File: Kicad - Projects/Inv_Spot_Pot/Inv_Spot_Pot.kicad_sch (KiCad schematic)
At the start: 29 parts, among them J1 Screw_Terminal_01x03, J2 PWM, J4 Current_Sense, J5 Temperature_Sense, Q1 40T120, Q2 40T120, T1 Transformer_1P_2S

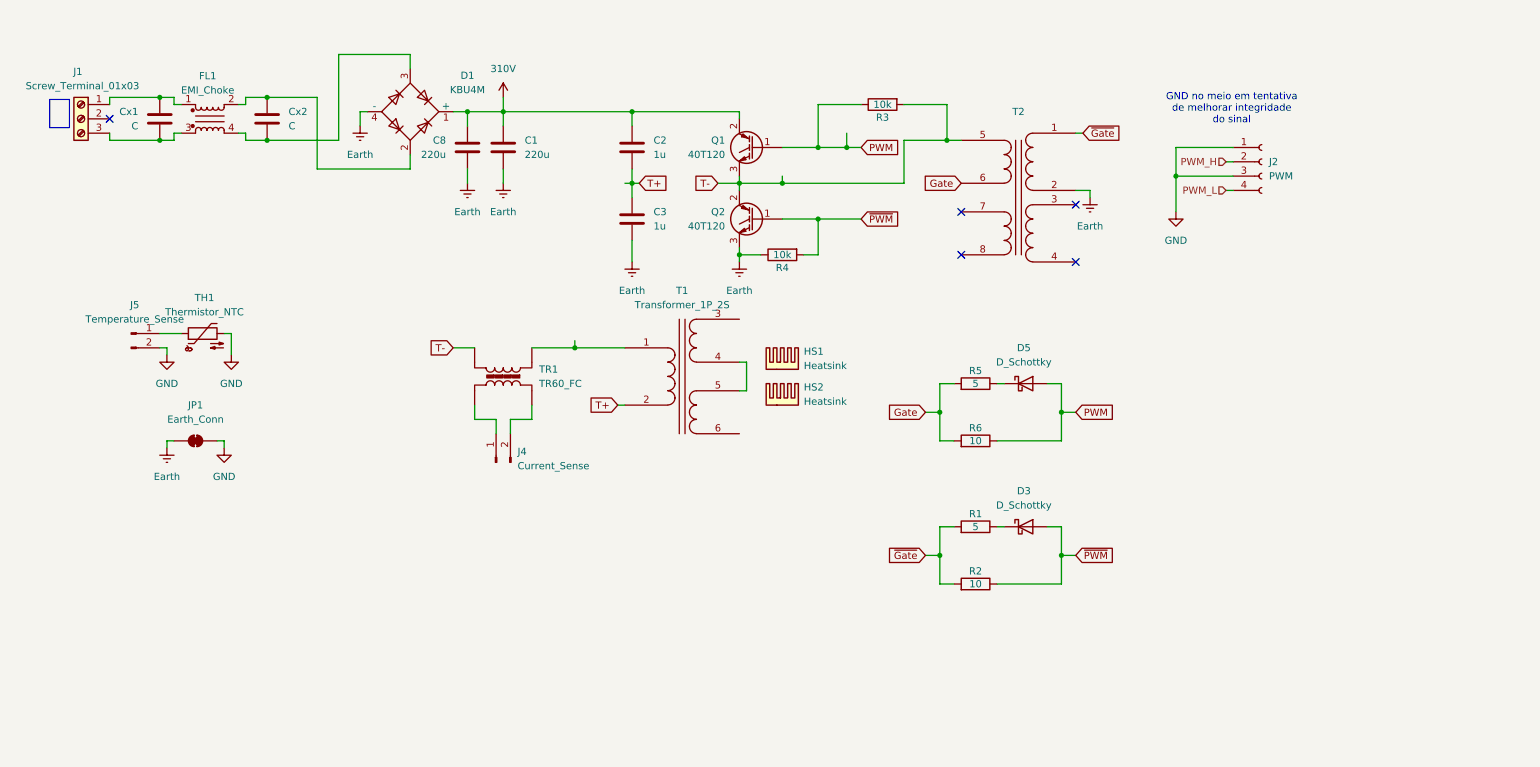
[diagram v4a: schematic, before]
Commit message: General Polishing
Removidos furos dos dissipadores que não serão utilizados, aberto espaço previsto para relé e circuito de tensão auxiliar

Falta ainda corrigir o footprint do transformador (bobinar) e a placa base de display que será utilizada
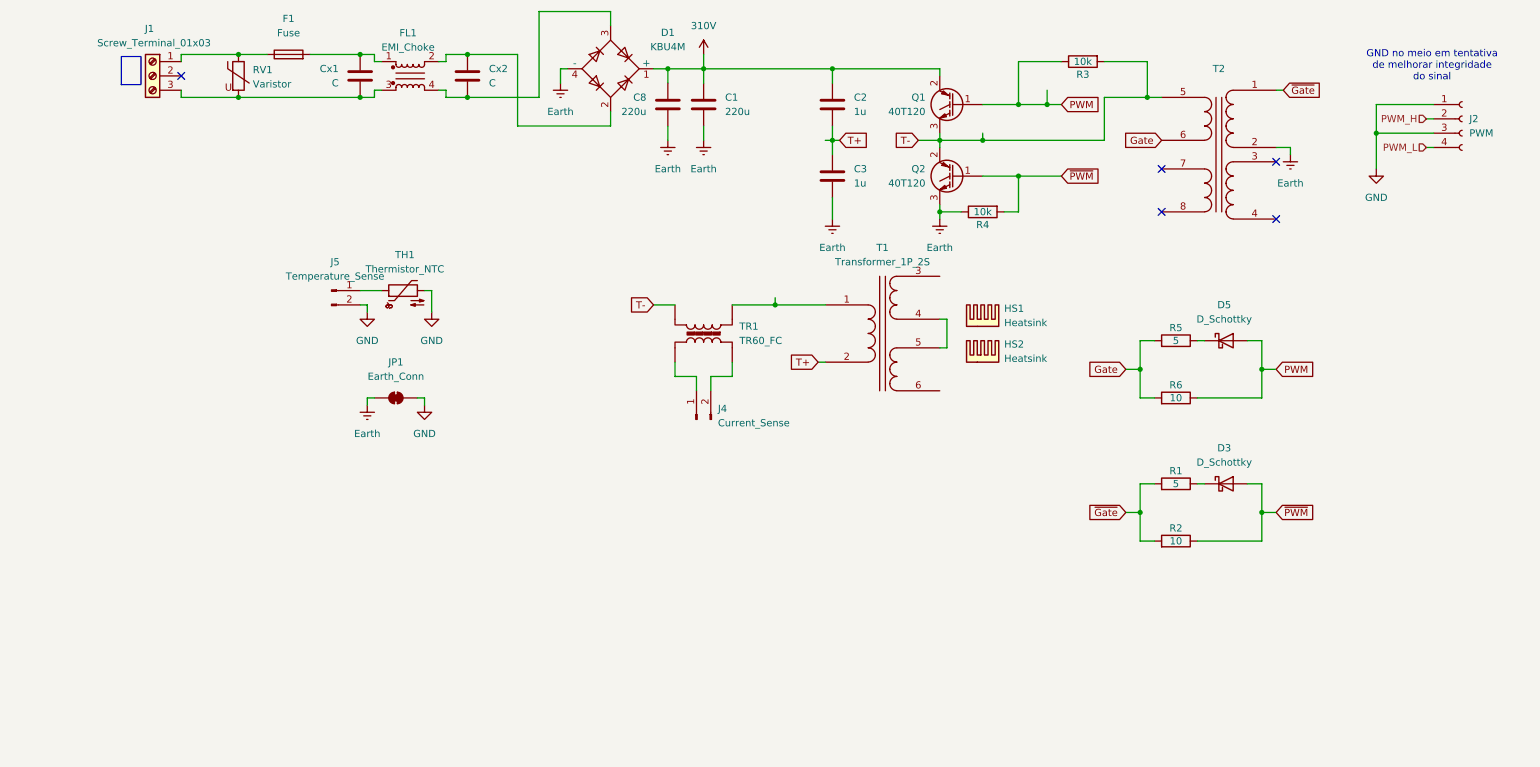
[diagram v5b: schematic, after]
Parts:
- added F1: Fuse, Fuse:Fuseholder_Clip-5x20mm_Schurter_CQM_Inline_P20.60x5.00mm_D1.00mm_Horizontal, symbol Device:Fuse
- added RV1: Varistor, Varistor:RV_Disc_D7mm_W3.4mm_P5mm, symbol Device:Varistor
- J2: footprint Connector_JST:JST_VH_B4P-VH-B_1x04_P3.96mm_Vertical -> Connector_PinHeader_2.00mm:PinHeader_1x04_P2.00mm_Vertical
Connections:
- net at Cx1.1, FL1.1: now also F1.2; no longer J1.1 (Pin_1)
- net at Cx1.2, FL1.3, J1.3 (Pin_3): now also RV1.2
- new net: F1.1, J1.1 (Pin_1), RV1.1
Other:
- moved on the sheet: C1, C2, C3, C8, Cx1, Cx2, D1, D3, D5, FL1, HS1, HS2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

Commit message: Adicionando Fonte Auxiliar
Fonte auxiliar com topologia flyback dimencionada, falta criar o footprint do transformador, abrir o espaço na placa e finalizar o roteamento dos componentes
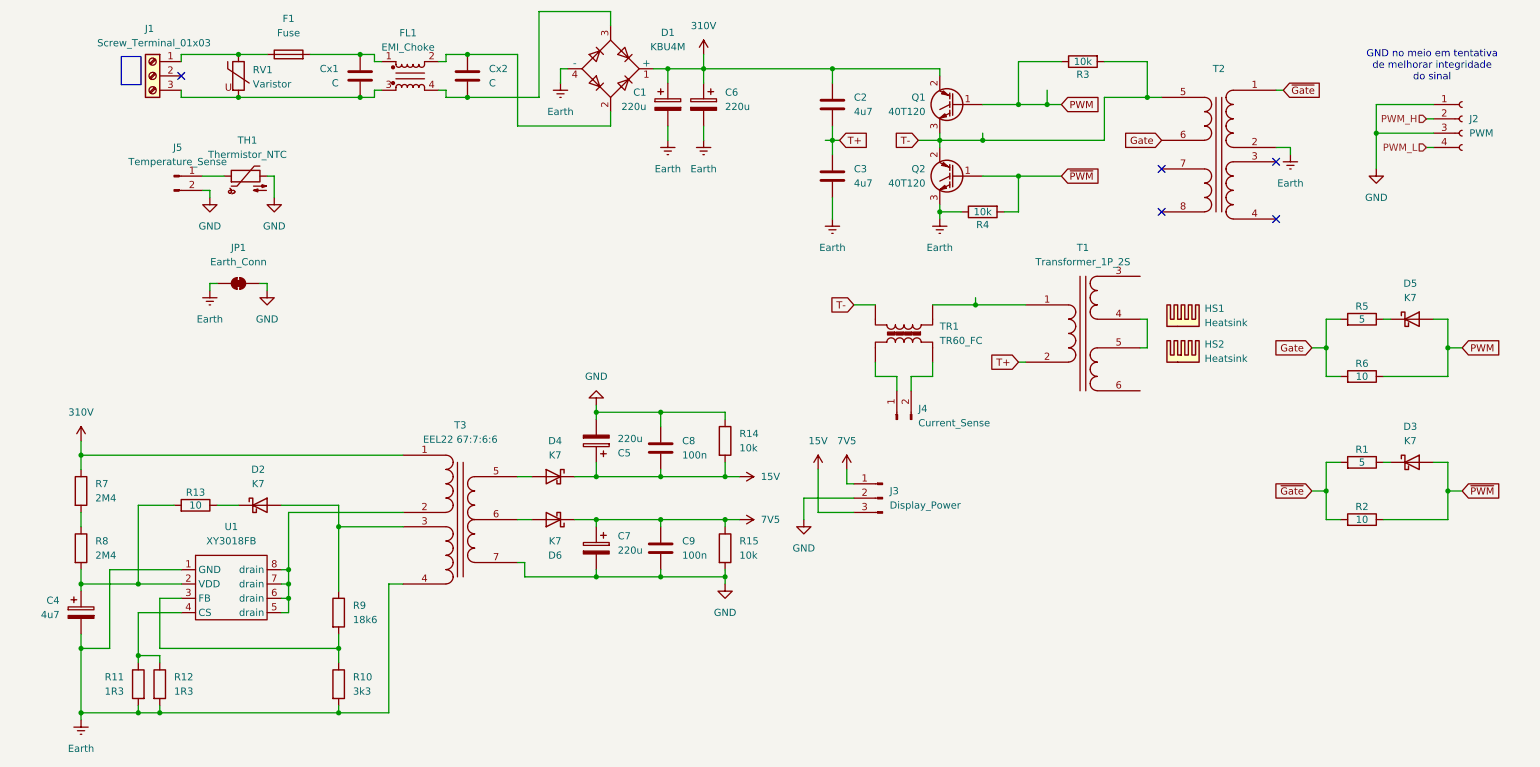
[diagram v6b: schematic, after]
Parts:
- removed C1: 220u, Capacitor_THT:C_Radial_D16.0mm_H25.0mm_P7.50mm, symbol Device:C
- added C1, C6: 220u, Capacitor_THT:C_Radial_D16.0mm_H25.0mm_P7.50mm, symbol Device:C_Polarized
- added C4: 4u7, Capacitor_THT:CP_Radial_D8.0mm_P3.50mm, symbol Device:C_Polarized
- added C5, C7: 220u, Capacitor_THT:CP_Radial_D8.0mm_P3.50mm, symbol Device:C_Polarized
- added C9: 100n, Capacitor_SMD:C_1206_3216Metric_Pad1.33x1.80mm_HandSolder, symbol Device:C
- added D2, D4, D6: K7, Diode_SMD:D_SOD-123F, symbol Device:D_Schottky
- added J3: Display_Power, Connector_PinHeader_2.00mm:PinHeader_1x03_P2.00mm_Vertical, symbol Connector:Conn_01x03_Pin
- added R10: 3k3, Resistor_SMD:R_1206_3216Metric_Pad1.30x1.75mm_HandSolder, symbol Device:R
- added R11, R12: 1R3, Resistor_SMD:R_1206_3216Metric_Pad1.30x1.75mm_HandSolder, symbol Device:R
- added R13: 10, Resistor_SMD:R_1206_3216Metric_Pad1.30x1.75mm_HandSolder, symbol Device:R
- added R14, R15: 10k, Resistor_SMD:R_1206_3216Metric_Pad1.30x1.75mm_HandSolder, symbol Device:R
- added R7, R8: 2M4, Resistor_SMD:R_1206_3216Metric_Pad1.30x1.75mm_HandSolder, symbol Device:R
- added R9: 18k6, Resistor_SMD:R_1206_3216Metric_Pad1.30x1.75mm_HandSolder, symbol Device:R
- added T3: EEL22 67:7:6:6, symbol Custom_Transformers:Transformer_1P_3S
- added U1: XY3018FB, Package_SO:SOIC-8_3.9x4.9mm_P1.27mm, symbol Custom_ICs:XY3018FB
- C2, C3: value 1u -> 4u7
- C8: value 220u -> 100n; footprint Capacitor_THT:C_Radial_D16.0mm_H25.0mm_P7.50mm -> Capacitor_SMD:C_1206_3216Metric_Pad1.33x1.80mm_HandSolder
- D3, D5: value D_Schottky -> K7
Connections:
- net 310V: now also C1.1, C6.1, R7.1, T3.1; no longer C8.1
- net Earth: now also C1.2, C4.2, C6.2, R10.2, R11.2, R12.2, T3.4, U1.1 (GND); no longer C8.2
- net GND: now also C8.1, C5.2, C7.2, C9.2, J3.2 (Pin_2), R14.1, R15.2, T3.7
- new net: D2.2 (A), R9.1, T3.3
- new net: R10.1, R9.2, U1.3 (FB)
- new net: D6.2 (A), T3.6
- new net: D2.1 (K), R13.1
- new net: C4.1, R13.2, R8.2, U1.2 (VDD)
- new net: T3.2, U1.5 (drain), U1.6 (drain), U1.7 (drain), U1.8 (drain)
- new net: D4.2 (A), T3.5
- new net: R11.1, R12.1, U1.4 (CS)
- new net: R7.2, R8.1
- new net 15V: C5.1, C8.2, D4.1 (K), J3.3 (Pin_3), R14.2
- new net 7V5: C7.1, C9.1, D6.1 (K), J3.1 (Pin_1), R15.1
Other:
- moved on the sheet: D3, D5, HS1, HS2, J4, J5, JP1, R1, R2, R5, R6, T1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

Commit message: Adicionado Flyback (WIP)
Adicionado circuito auxiliar flyback - footprint ocupa bastante espaço e aumenta significativamente a altura da placa.

Revendo layout para tentar melhorar o particionamento da placa
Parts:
- added C10: 47u, Capacitor_THT:CP_Radial_D8.0mm_P3.50mm, symbol Device:C_Polarized
- R7, R8: footprint Resistor_SMD:R_1206_3216Metric_Pad1.30x1.75mm_HandSolder -> Resistor_THT:R_Axial_DIN0309_L9.0mm_D3.2mm_P12.70mm_Horizontal
- T3: footprint (none) -> Transformer_THT:Custom_Transformer-10P-EEL22_EE30_7
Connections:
- net 15V: now also C7.1, C9.1, D6.1 (K), J3.1 (Pin_1), R15.1; no longer C5.1, C8.2, D4.1 (K), J3.3 (Pin_3), R14.2
- net 310V: now also C10.1
- net 7V5: now also C5.1, C8.2, D4.1 (K), J3.3 (Pin_3), R14.2; no longer C7.1, C9.1, D6.1 (K), J3.1 (Pin_1), R15.1
- net Earth: now also C10.2
- net GND: now also T3.6; no longer T3.7
- net at D6.2 (A): now also T3.9; no longer T3.6
- net at D4.2 (A): now also T3.7; no longer T3.5
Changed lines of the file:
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@@
 	(wire
 		(pts
+			(xy 19.05 139.7) (xy 19.05 140.97)
+		)
+		(stroke
+			(width 0)
+			(type default)
+		)
+	)
+	(wire
+		(pts
 			(xy 118.11 50.8) (xy 118.11 53.34)
 		)
@@
 	(wire
 		(pts
+			(xy 19.05 132.08) (xy 19.05 129.54)
+		)
+		(stroke
+			(width 0)
+			(type default)
+		)
+	)
+	(wire
+		(pts
 			(xy 176.53 72.39) (xy 176.53 73.66)
 		)
@@
 	(wire
 		(pts
+			(xy 19.05 129.54) (xy 24.13 129.54)
+		)
+		(stroke
+			(width 0)
+			(type default)
+		)
+	)
+	(wire
+		(pts
 			(xy 157.48 73.66) (xy 158.75 73.66)
 		)
@@
 			)
 		)
-		(property "Value" "15V"
+		(property "Value" "7V5"
 			(at 144.78 133.3499 90)
 			(effects
@@
 			)
 		)
-		(property "Value" "7V5"
+		(property "Value" "15V"
 			(at 160.02 127 0)
 			(effects
@@
 			)
 		)
-		(property "Footprint" ""
+		(property "Footprint" "Transformer_THT:Custom_Transformer-10P-EEL22_EE30_7"
 			(at 91.44 129.54 0)
 			(effects
@@
 		(pin "6"
 		)
-		(pin "5"
+		(pin "9"
 		)
 		(pin "7"
@@
 	(symbol
 		(lib_id "power:Earth")
+		(at 19.05 140.97 0)
+		(unit 1)
+		(exclude_from_sim no)
+		(in_bom yes)
+		(on_board yes)
+		(dnp no)
+		(fields_autoplaced yes)
+		(property "Reference" "#PWR022"
+			(at 19.05 147.32 0)
+			(effects
+				(font
+					(size 1.27 1.27)
+				)
+				(hide yes)
+			)
+		)
+		(property "Value" "Earth"
+			(at 19.05 146.05 0)
+			(effects
+				(font
+					(size 1.27 1.27)
+				)
+			)
+		)
+		(property "Footprint" ""
+			(at 19.05 140.97 0)
+			(effects
+				(font
+					(size 1.27 1.27)
+				)
+				(hide yes)
+			)
+		)
+		(property "Datasheet" "~"
+			(at 19.05 140.97 0)
+			(effects
+				(font
+					(size 1.27 1.27)
+				)
+				(hide yes)
+			)
+		)
+		(property "Description" "Power symbol creates a global label with name \"Earth\""
+			(at 19.05 140.97 0)
+			(effects
+				(font
+					(size 1.27 1.27)
+				)
+				(hide yes)
+			)
+		)
+		(pin "1"
+		)
+		(instances
+			(project "Inv_Spot_Pot"
+				(path "/e27abe51-96c0-4fdf-ba00-b5a281cd0e9c"
+					(reference "#PWR022")
+					(unit 1)
+				)
+			)
+		)
+	)
+	(symbol
+		(lib_id "power:Earth")
 		(at 128.27 73.66 0)
 		(unit 1)
@@
 			)
 		)
-		(property "Footprint" "Resistor_SMD:R_1206_3216Metric_Pad1.30x1.75mm_HandSolder"
+		(property "Footprint" "Resistor_THT:R_Axial_DIN0309_L9.0mm_D3.2mm_P12.70mm_Horizontal"
 			(at 22.352 146.05 90)
 			(effects
@@
 	)
 	(symbol
+		(lib_id "Device:C_Polarized")
+		(at 19.05 135.89 0)
+		(unit 1)
+		(exclude_from_sim no)
+		(in_bom yes)
+		(on_board yes)
+		(dnp no)
+		(property "Reference" "C10"
+			(at 16.51 130.81 0)
+			(effects
+				(font
+					(size 1.27 1.27)
+				)
+				(justify right)
+			)
+		)
+		(property "Value" "47u"
+			(at 16.51 133.35 0)
+			(effects
+				(font
+					(size 1.27 1.27)
+				)
+				(justify right)
+			)
+		)
+		(property "Footprint" "Capacitor_THT:CP_Radial_D8.0mm_P3.50mm"
+			(at 20.0152 139.7 0)
+			(effects
+				(font
+					(size 1.27 1.27)
+				)
+				(hide yes)
+			)
+		)
+		(property "Datasheet" "~"
+			(at 19.05 135.89 0)
+			(effects
+				(font
+					(size 1.27 1.27)
+				)
+				(hide yes)
+			)
+		)
+		(property "Description" "Polarized capacitor"
+			(at 19.05 135.89 0)
+			(effects
+				(font
+					(size 1.27 1.27)
+				)
+				(hide yes)
+			)
+		)
+		(pin "2"
+		)
+		(pin "1"
+		)
+		(instances
+			(project "Inv_Spot_Pot"
+				(path "/e27abe51-96c0-4fdf-ba00-b5a281cd0e9c"
+					(reference "C10")
+					(unit 1)
+				)
+			)
+		)
+	)
+	(symbol
 		(lib_id "Device:R")
 		(at 184.15 86.36 90)
@@
 			)
 		)
-		(property "Footprint" "Resistor_SMD:R_1206_3216Metric_Pad1.30x1.75mm_HandSolder"
+		(property "Footprint" "Resistor_THT:R_Axial_DIN0309_L9.0mm_D3.2mm_P12.70mm_Horizontal"
 			(at 22.352 135.89 90)
 			(effects
@@
 			)
 		)
-		(property "Value" "15V"
+		(property "Value" "7V5"
 			(at 154.94 127 0)
 			(effects
@@
 			)
 		)
-		(property "Value" "7V5"
+		(property "Value" "15V"
 			(at 144.78 140.9699 90)
 			(effects

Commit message: Capacitores Ajustados
Ajustado o footprint dos capacitores divisores de tensão (poly) para ser coerente com os 4u7 escolhidos

Também foi adicionada uma distância entre o transformador para abrir espaço a uma ponteira de corrente
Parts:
- C2, C3: footprint Capacitor_THT:C_Rect_L16.5mm_W4.7mm_P15.00mm_MKT -> Capacitor_THT:C_Rect_L24.0mm_W7.0mm_P22.50mm_MKT
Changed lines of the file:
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@@
 			)
 		)
-		(property "Footprint" "Capacitor_THT:C_Rect_L16.5mm_W4.7mm_P15.00mm_MKT"
+		(property "Footprint" "Capacitor_THT:C_Rect_L24.0mm_W7.0mm_P22.50mm_MKT"
 			(at 158.4452 83.82 0)
 			(effects
@@
 			)
 		)
-		(property "Footprint" "Capacitor_THT:C_Rect_L16.5mm_W4.7mm_P15.00mm_MKT"
+		(property "Footprint" "Capacitor_THT:C_Rect_L24.0mm_W7.0mm_P22.50mm_MKT"
 			(at 158.4452 71.12 0)
 			(effects
